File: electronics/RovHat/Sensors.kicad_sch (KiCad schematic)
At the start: 1 part, among them J201 Conn_01x10

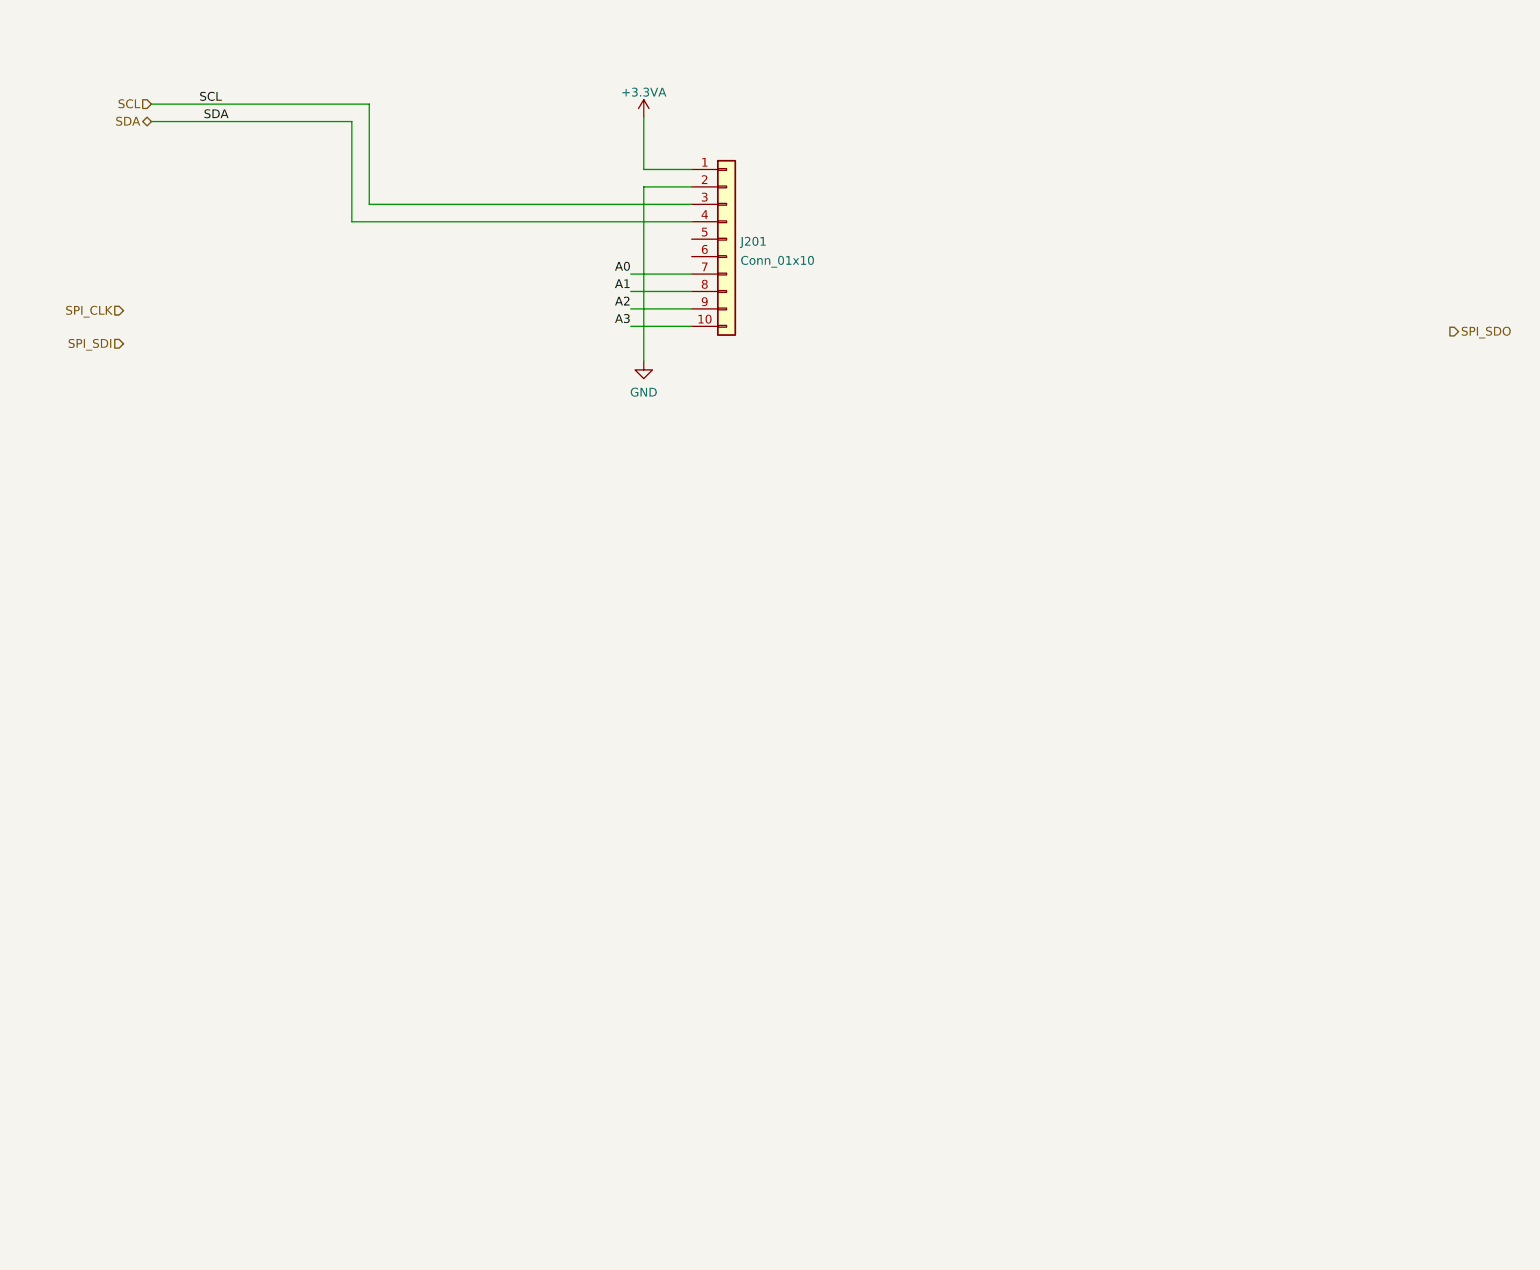
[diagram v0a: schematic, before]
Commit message: Changed To RPI Pico Module
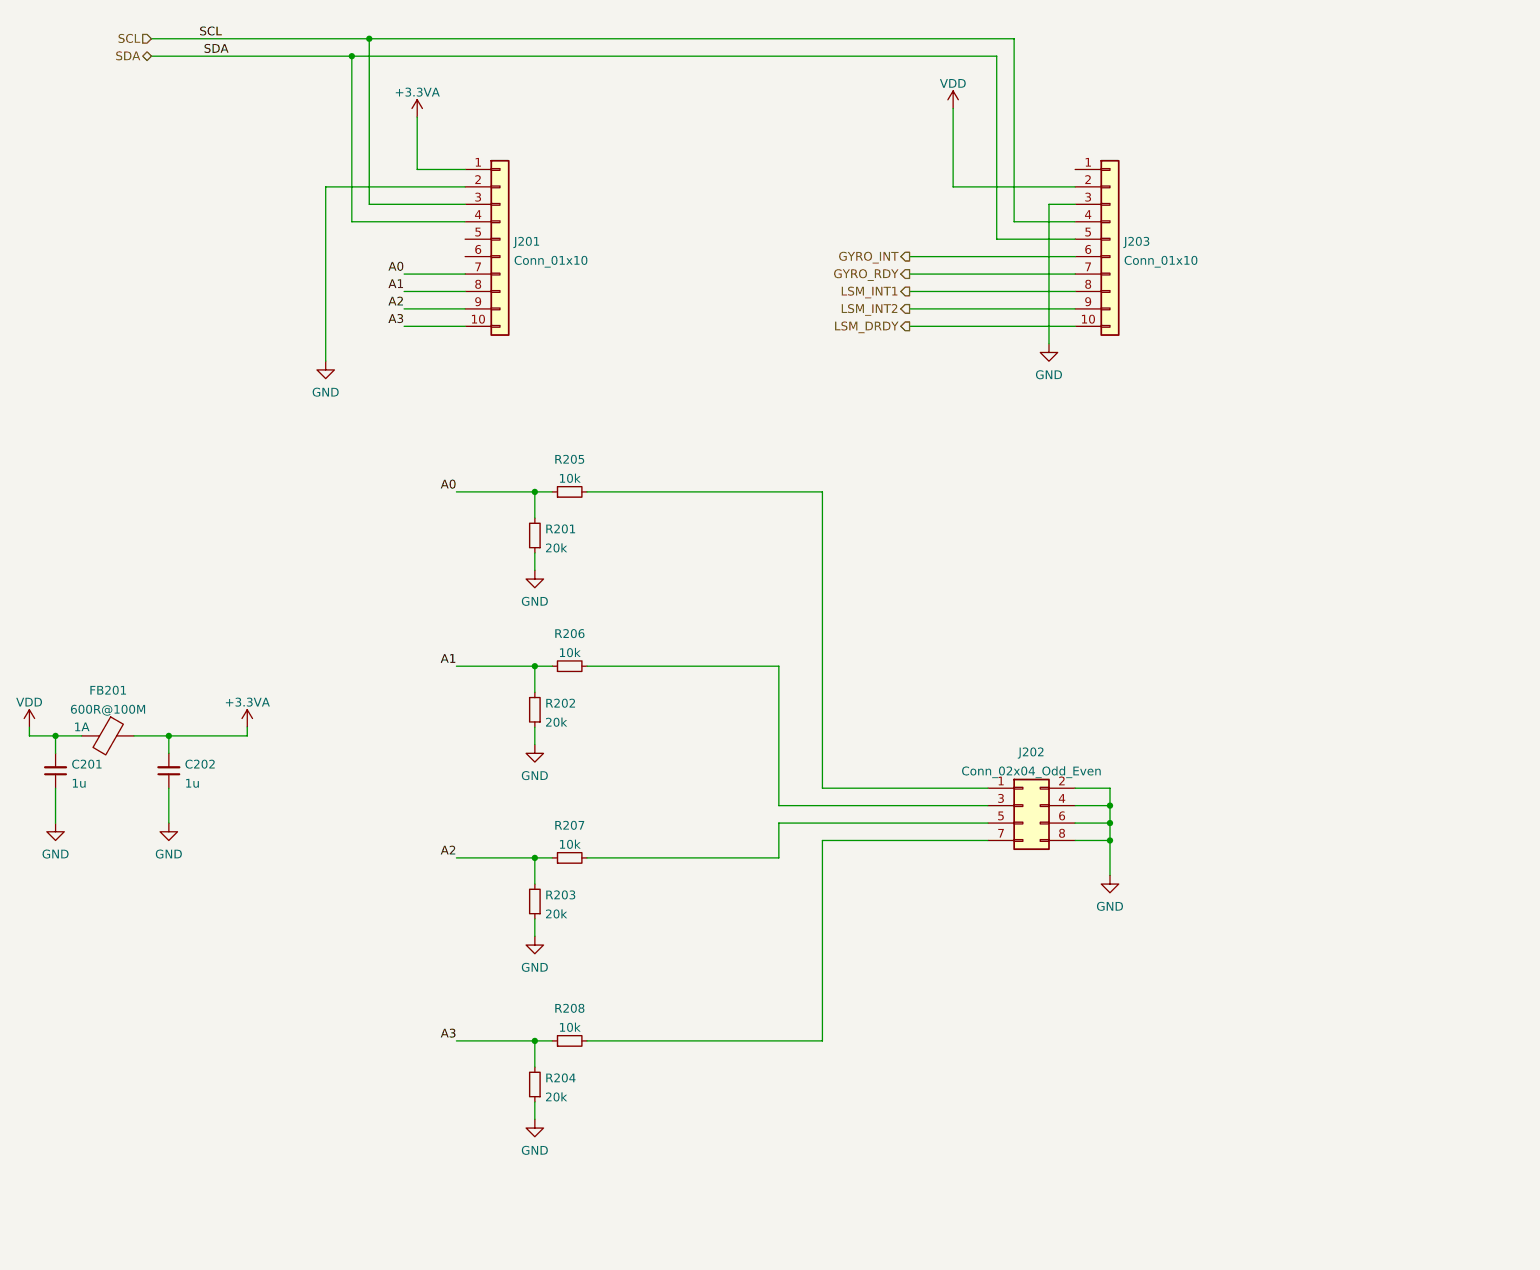
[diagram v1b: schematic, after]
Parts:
- added C201: 1u, Capacitor_SMD:C_0402_1005Metric, symbol Device:C_Small
- added C202: 1u, Capacitor_SMD:C_0603_1608Metric, symbol Device:C_Small
- added FB201: 600R@100M, Inductor_SMD:L_0805_2012Metric, symbol Device:FerriteBead
- added J202: Conn_02x04_Odd_Even, Connector_PinHeader_2.54mm:PinHeader_2x04_P2.54mm_Vertical, symbol Connector_Generic:Conn_02x04_Odd_Even
- added J203: Conn_01x10, Connector_PinHeader_2.54mm:PinHeader_1x10_P2.54mm_Vertical, symbol Connector_Generic:Conn_01x10
- added R201, R202, R203, R204: 20k, Resistor_SMD:R_0402_1005Metric, symbol Device:R_Small
- added R205, R206, R207, R208: 10k, Resistor_SMD:R_0402_1005Metric, symbol Device:R_Small
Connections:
- net +3.3VA: now also C202.2, FB201.1
- net A0: now also R201.2, R205.1
- net A1: now also R202.2, R206.1
- net A2: now also R203.2, R207.1
- net A3: now also R204.2, R208.1
- net GND: now also C201.1, C202.1, J202.2 (Pin_2), J202.4 (Pin_4), J202.6 (Pin_6), J202.8 (Pin_8), J203.3 (Pin_3), R201.1, R202.1, R203.1, R204.1
- net SCL: now also J203.4 (Pin_4)
- net SDA: now also J203.5 (Pin_5)
- new net: J202.1 (Pin_1), R205.2
- new net: J202.3 (Pin_3), R206.2
- new net: J202.5 (Pin_5), R207.2
- new net: J202.7 (Pin_7), R208.2
- new net GYRO_INT: J203.6 (Pin_6)
- new net GYRO_RDY: J203.7 (Pin_7)
- new net LSM_DRDY: J203.10 (Pin_10)
- new net LSM_INT1: J203.8 (Pin_8)
- new net LSM_INT2: J203.9 (Pin_9)
- new net VDD: C201.2, FB201.2, J203.2 (Pin_2)
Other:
- moved on the sheet: J201

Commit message: Layout Done first level
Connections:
- no-connect marks 0 -> 3
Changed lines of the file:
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@@
   (junction (at 185.42 133.35) (diameter 0) (color 0 0 0 0)
   )
+  (junction (at 52.07 118.11) (diameter 0) (color 0 0 0 0)
+  )
   (junction (at 48.26 118.11) (diameter 0) (color 0 0 0 0)
   )
@@
   (junction (at 31.75 118.11) (diameter 0) (color 0 0 0 0)
   )
+  (no_connect (at 91.44 45.72))
+  (no_connect (at 91.44 48.26))
+  (no_connect (at 180.34 35.56))
   (wire (pts (xy 156.21 53.34) (xy 180.34 53.34))
     (stroke (width 0) (type default) (color 0 0 0 0))
@@
     (stroke (width 0) (type default) (color 0 0 0 0))
   )
+  (wire (pts (xy 52.07 116.84) (xy 52.07 118.11))
+    (stroke (width 0) (type default) (color 0 0 0 0))
+  )
   (wire (pts (xy 101.6 107.95) (xy 101.6 111.76))
     (stroke (width 0) (type default) (color 0 0 0 0))
@@
     (stroke (width 0) (type default) (color 0 0 0 0))
   )
-  (wire (pts (xy 48.26 118.11) (xy 59.69 118.11))
+  (wire (pts (xy 48.26 118.11) (xy 52.07 118.11))
     (stroke (width 0) (type default) (color 0 0 0 0))
   )
@@
   )
   (wire (pts (xy 101.6 135.89) (xy 104.14 135.89))
+    (stroke (width 0) (type default) (color 0 0 0 0))
+  )
+  (wire (pts (xy 52.07 118.11) (xy 59.69 118.11))
     (stroke (width 0) (type default) (color 0 0 0 0))
   )
@@
       (effects (font (size 1.27 1.27)) hide)
     )
+    (pin "1")
+  )
+  (symbol (lib_id "power:PWR_FLAG") (at 52.07 116.84 0) (unit 1)
+    (in_bom yes) (on_board yes) (fields_autoplaced)
+    (property "Reference" "#FLG0104" (id 0) (at 52.07 114.935 0)
+      (effects (font (size 1.27 1.27)) hide)
+    )
+    (property "Value" "PWR_FLAG" (id 1) (at 52.07 113.2355 0)
+      (effects (font (size 1.27 1.27)) hide)
+    )
+    (property "Footprint" "" (id 2) (at 52.07 116.84 0)
+      (effects (font (size 1.27 1.27)) hide)
+    )
+    (property "Datasheet" "~" (id 3) (at 52.07 116.84 0)
+      (effects (font (size 1.27 1.27)) hide)
+    )

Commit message: Fabrication commit
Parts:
- removed C201: 1u, Capacitor_SMD:C_0402_1005Metric, symbol Device:C_Small
- removed C202: 1u, Capacitor_SMD:C_0603_1608Metric, symbol Device:C_Small
- removed FB201: 600R@100M, Inductor_SMD:L_0805_2012Metric, symbol Device:FerriteBead
- added R209, R210, R211: 4k7, Resistor_SMD:R_0603_1608Metric, symbol Device:R_Small
- J201: value Conn_01x10 -> ADS1115
- J202: value Conn_02x04_Odd_Even -> ANALOG INPUT
- J203: value Conn_01x10 -> GYRO
- R201, R202, R203, R204, R205, R206, R207, R208: footprint Resistor_SMD:R_0402_1005Metric -> Resistor_SMD:R_0603_1608Metric
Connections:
- net +3.3VA is gone; now on net VDD: J201.1 (Pin_1)
- net SCL: now also R210.1
- net SDA: now also R211.1
- net VDD: now also R209.2, R210.2, R211.2
- net at J201.5 (Pin_5): now also R209.1
- net ADS_RDY: now reaches J201.6 (Pin_6)
- net +5V: now reaches J203.1 (Pin_1)
- no-connect marks 3 -> 0
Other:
- moved on the sheet: J201, J202, J203, R201, R202, R203, R204, R205, R206, R207, R208

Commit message: Fabrication commit 2
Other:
- company: (none) -> Findersee
- title: (none) -> ROV RPI PICO HAT
- moved on the sheet: J201, J202, J203, R201, R202, R203, R204, R205, R206, R207, R208, R209

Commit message: Final Version
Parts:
- added J204: I2C EXPAND, Connector_PinHeader_2.54mm:PinHeader_1x04_P2.54mm_Vertical, symbol Connector_Generic:Conn_01x04
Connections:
- net GND: now also J204.4 (Pin_4)
- net SCL: now also J204.2 (Pin_2)
- net SDA: now also J204.3 (Pin_3)
- net VDD: now also J204.1 (Pin_1)
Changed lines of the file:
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@@
   (junction (at 110.49 27.94) (diameter 0) (color 0 0 0 0)
   )
+  (junction (at 200.66 27.94) (diameter 0) (color 0 0 0 0)
+  )
   (junction (at 134.62 96.52) (diameter 0) (color 0 0 0 0)
   )
@@
   (junction (at 119.38 30.48) (diameter 0) (color 0 0 0 0)
   )
+  (junction (at 198.12 30.48) (diameter 0) (color 0 0 0 0)
+  )
   (junction (at 50.8 144.78) (diameter 0) (color 0 0 0 0)
   )
@@
     (stroke (width 0) (type default) (color 0 0 0 0))
   )
+  (wire (pts (xy 222.25 33.02) (xy 218.44 33.02))
+    (stroke (width 0) (type default) (color 0 0 0 0))
+  )
   (wire (pts (xy 50.8 144.78) (xy 50.8 147.32))
     (stroke (width 0) (type default) (color 0 0 0 0))
@@
     (stroke (width 0) (type default) (color 0 0 0 0))
   )
+  (wire (pts (xy 218.44 22.86) (xy 218.44 25.4))
+    (stroke (width 0) (type default) (color 0 0 0 0))
+  )
   (wire (pts (xy 185.42 119.38) (xy 185.42 104.14))
     (stroke (width 0) (type default) (color 0 0 0 0))
@@
     (stroke (width 0) (type default) (color 0 0 0 0))
   )
+  (wire (pts (xy 198.12 30.48) (xy 222.25 30.48))
+    (stroke (width 0) (type default) (color 0 0 0 0))
+  )
   (wire (pts (xy 110.49 17.78) (xy 110.49 19.05))
     (stroke (width 0) (type default) (color 0 0 0 0))
@@
     (stroke (width 0) (type default) (color 0 0 0 0))
   )
+  (wire (pts (xy 218.44 33.02) (xy 218.44 36.83))
+    (stroke (width 0) (type default) (color 0 0 0 0))
+  )
   (wire (pts (xy 68.58 142.24) (xy 99.06 142.24))
     (stroke (width 0) (type default) (color 0 0 0 0))
@@
     (stroke (width 0) (type default) (color 0 0 0 0))
   )
+  (wire (pts (xy 200.66 27.94) (xy 222.25 27.94))
+    (stroke (width 0) (type default) (color 0 0 0 0))
+  )
   (wire (pts (xy 99.06 144.78) (xy 68.58 144.78))
+    (stroke (width 0) (type default) (color 0 0 0 0))
+  )
+  (wire (pts (xy 222.25 25.4) (xy 218.44 25.4))
     (stroke (width 0) (type default) (color 0 0 0 0))
   )
@@
     )
     (property "Datasheet" "" (id 3) (at 90.17 38.1 0)
+      (effects (font (size 1.27 1.27)) hide)
+    )
+    (pin "1")
+  )
+  (symbol (lib_id "power:GND") (at 218.44 36.83 0) (unit 1)
+    (in_bom yes) (on_board yes) (fields_autoplaced)
+    (property "Reference" "#PWR0208" (id 0) (at 218.44 43.18 0)
+      (effects (font (size 1.27 1.27)) hide)
+    )
+    (property "Value" "GND" (id 1) (at 218.44 41.3925 0))
+    (property "Footprint" "" (id 2) (at 218.44 36.83 0)
+      (effects (font (size 1.27 1.27)) hide)
+    )
+    (property "Datasheet" "" (id 3) (at 218.44 36.83 0)
       (effects (font (size 1.27 1.27)) hide)
     )
@@
     (pin "2")
   )
+  (symbol (lib_id "Connector_Generic:Conn_01x04") (at 227.33 27.94 0) (unit 1)
+    (in_bom yes) (on_board yes) (fields_autoplaced)
+    (property "Reference" "J204" (id 0) (at 229.362 28.3015 0)
+      (effects (font (size 1.27 1.27)) (justify left))
+    )
+    (property "Value" "I2C EXPAND" (id 1) (at 229.362 31.0766 0)
+      (effects (font (size 1.27 1.27)) (justify left))
+    )
+    (property "Footprint" "Connector_PinHeader_2.54mm:PinHeader_1x04_P2.54mm_Vertical" (id 2) (at 227.33 27.94 0)
+      (effects (font (size 1.27 1.27)) hide)
+    )
+    (property "Datasheet" "~" (id 3) (at 227.33 27.94 0)
+      (effects (font (size 1.27 1.27)) hide)
+    )
+    (pin "1")
+    (pin "2")
+    (pin "3")
+    (pin "4")
+  )
   (symbol (lib_id "power:GND") (at 90.17 72.39 0) (unit 1)
     (in_bom yes) (on_board yes) (fields_autoplaced)
@@
       (effects (font (size 1.27 1.27)) hide)
     )
+    (pin "1")
+  )
+  (symbol (lib_id "power:VDD") (at 218.44 22.86 0) (unit 1)
+    (in_bom yes) (on_board yes) (fields_autoplaced)
+    (property "Reference" "#PWR0201" (id 0) (at 218.44 26.67 0)
+      (effects (font (size 1.27 1.27)) hide)
+    )
+    (property "Value" "VDD" (id 1) (at 218.44 19.2555 0))
+    (property "Footprint" "" (id 2) (at 218.44 22.86 0)
+      (effects (font (size 1.27 1.27)) hide)
+    )
+    (property "Datasheet" "" (id 3) (at 218.44 22.86 0)
+      (effects (font (size 1.27 1.27)) hide)
+    )
